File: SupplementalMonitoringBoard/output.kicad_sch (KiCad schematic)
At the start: 7 parts

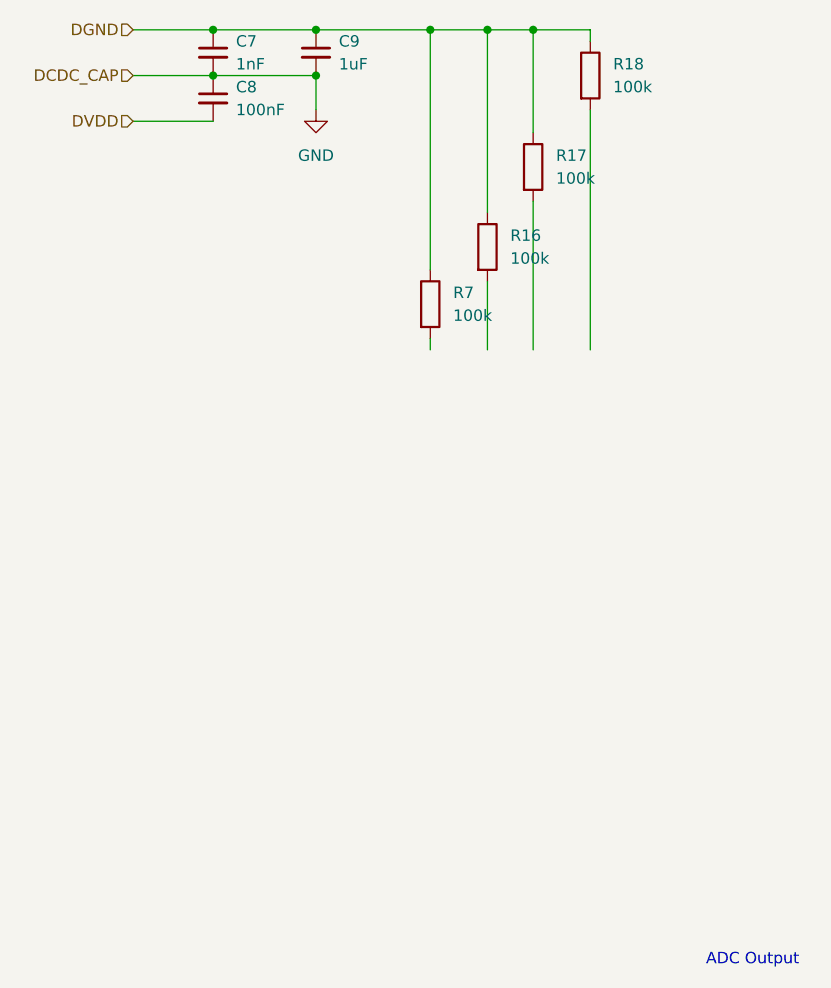
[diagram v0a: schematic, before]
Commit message: Supplemental Monitoring Board Changes
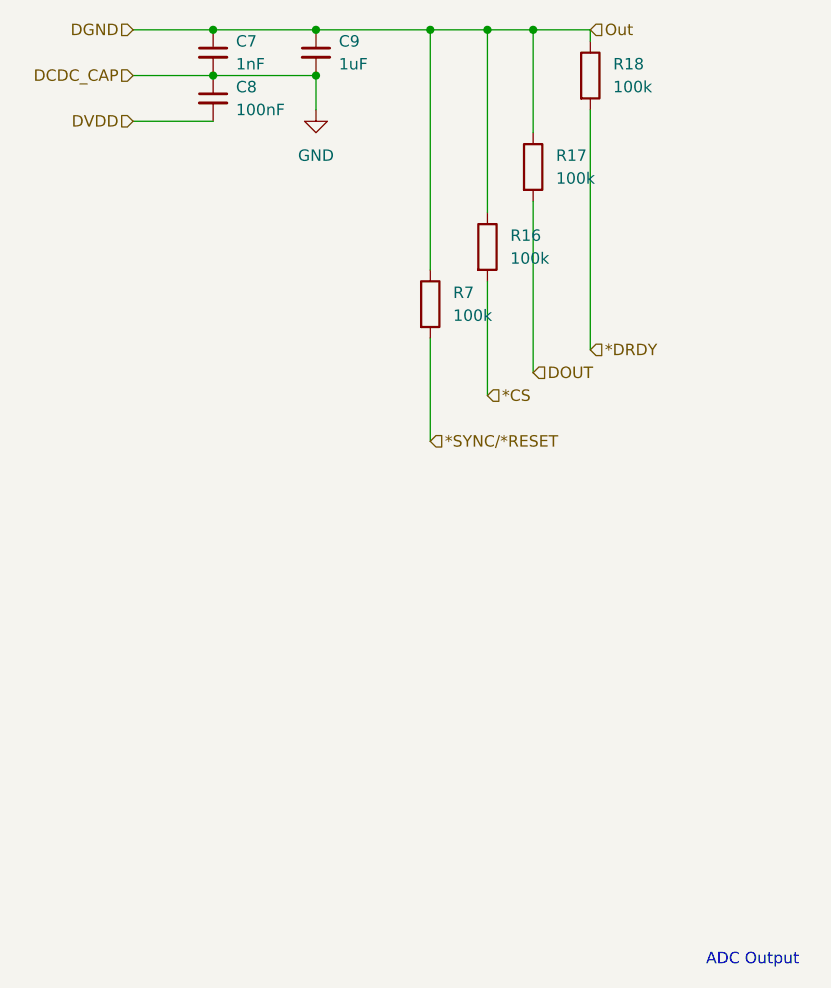
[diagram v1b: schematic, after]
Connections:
- net *CS: now reaches R16.2
- net *DRDY: now reaches R18.2
- net *SYNC/*RESET: now reaches R7.2
- net DOUT: now reaches R17.2
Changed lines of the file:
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@@
 	(wire
 		(pts
-			(xy 162.56 114.3) (xy 162.56 121.92)
+			(xy 162.56 114.3) (xy 162.56 127)
 		)
 		(stroke
@@
 	(wire
 		(pts
-			(xy 167.64 105.41) (xy 167.64 121.92)
+			(xy 167.64 105.41) (xy 167.64 124.46)
 		)
 		(stroke
@@
 	(wire
 		(pts
-			(xy 156.21 120.65) (xy 156.21 121.92)
+			(xy 156.21 120.65) (xy 156.21 132.08)
 		)
 		(stroke
@@
 		)
 	)
+	(hierarchical_label "*CS"
+		(shape input)
+		(at 162.56 127 0)
+		(fields_autoplaced yes)
+		(effects
+			(font
+				(size 1.27 1.27)
+			)
+			(justify left)
+		)
+	)
+	(hierarchical_label "*DRDY"
+		(shape input)
+		(at 173.99 121.92 0)
+		(fields_autoplaced yes)
+		(effects
+			(font
+				(size 1.27 1.27)
+			)
+			(justify left)
+		)
+	)
+	(hierarchical_label "*SYNC{slash}*RESET"
+		(shape input)
+		(at 156.21 132.08 0)
+		(fields_autoplaced yes)
+		(effects
+			(font
+				(size 1.27 1.27)
+			)
+			(justify left)
+		)
+	)
 	(hierarchical_label "DCDC_CAP"
 		(shape input)
@@
 		)
 	)
+	(hierarchical_label "DOUT"
+		(shape input)
+		(at 167.64 124.46 0)
+		(fields_autoplaced yes)
+		(effects
+			(font
+				(size 1.27 1.27)
+			)
+			(justify left)
+		)
+	)
+	(hierarchical_label "Out"
+		(shape input)
+		(at 173.99 86.36 0)
+		(fields_autoplaced yes)
+		(effects
+			(font
+				(size 1.27 1.27)
+			)
+			(justify left)
+		)
+	)

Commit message: thing
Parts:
- C7, C8, C9: footprint (none) -> Capacitor_SMD:C_0805_2012Metric
- R16, R17, R18, R7: footprint (none) -> Resistor_SMD:R_0805_2012Metric
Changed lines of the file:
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@@
 			)
 		)
-		(property "Footprint" ""
+		(property "Footprint" "Resistor_SMD:R_0805_2012Metric"
 			(at 160.782 110.49 90)
 			(effects
@@
 			)
 		)
-		(property "Footprint" ""
+		(property "Footprint" "Capacitor_SMD:C_0805_2012Metric"
 			(at 143.51 88.9 0)
 			(effects
@@
 			)
 		)
-		(property "Footprint" ""
+		(property "Footprint" "Resistor_SMD:R_0805_2012Metric"
 			(at 172.212 91.44 90)
 			(effects
@@
 			)
 		)
-		(property "Footprint" ""
+		(property "Footprint" "Capacitor_SMD:C_0805_2012Metric"
 			(at 132.08 93.98 0)
 			(effects
@@
 			)
 		)
-		(property "Footprint" ""
+		(property "Footprint" "Resistor_SMD:R_0805_2012Metric"
 			(at 154.432 116.84 90)
 			(effects
@@
 			)
 		)
-		(property "Footprint" ""
+		(property "Footprint" "Capacitor_SMD:C_0805_2012Metric"
 			(at 132.08 88.9 0)
 			(effects
@@
 			)
 		)
-		(property "Footprint" ""
+		(property "Footprint" "Resistor_SMD:R_0805_2012Metric"
 			(at 165.862 101.6 90)
 			(effects

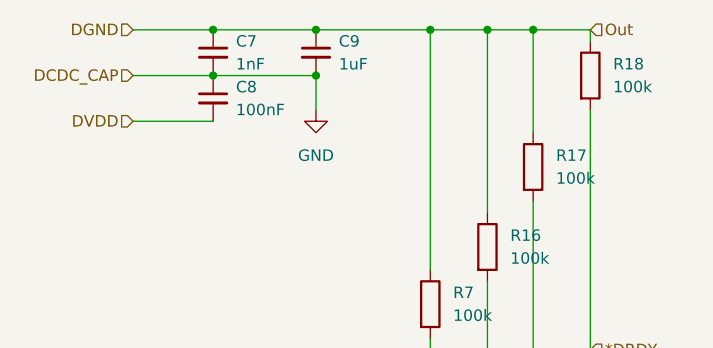
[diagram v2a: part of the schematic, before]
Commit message: Adressed Reviews - Supplemental Monitoring Board
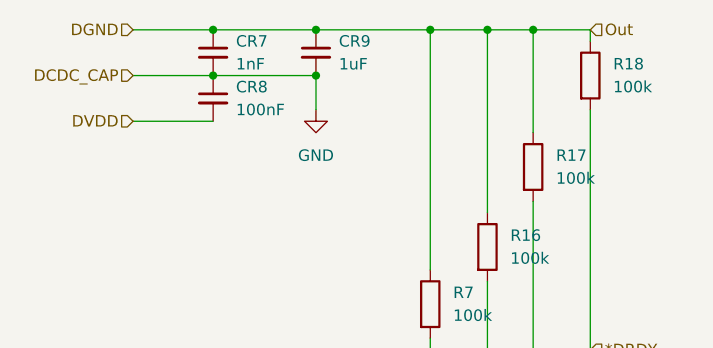
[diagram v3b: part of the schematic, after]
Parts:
- renumbered C7 to CR7, C8 to CR8, C9 to CR9
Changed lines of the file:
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@@
 		(dnp no)
 		(fields_autoplaced yes)
-		(property "Reference" "C9"
+		(property "Reference" "CR9"
 			(at 146.05 87.6362 0)
 			(effects
@@
 			(project "SupplementalMonitoringBoard"
 				(path "/aa0415d0-3287-4bc4-9a8e-766ada9ace2f/1227ac4e-31e5-4c8e-a2fc-47c8873f33fc"
-					(reference "C9")
+					(reference "CR9")
 					(unit 1)
 				)
@@
 		(dnp no)
 		(fields_autoplaced yes)
-		(property "Reference" "C8"
+		(property "Reference" "CR8"
 			(at 134.62 92.7162 0)
 			(effects
@@
 			(project "SupplementalMonitoringBoard"
 				(path "/aa0415d0-3287-4bc4-9a8e-766ada9ace2f/1227ac4e-31e5-4c8e-a2fc-47c8873f33fc"
-					(reference "C8")
+					(reference "CR8")
 					(unit 1)
 				)
@@
 		(dnp no)
 		(fields_autoplaced yes)
-		(property "Reference" "C7"
+		(property "Reference" "CR7"
 			(at 134.62 87.6362 0)
 			(effects
@@
 			(project "SupplementalMonitoringBoard"
 				(path "/aa0415d0-3287-4bc4-9a8e-766ada9ace2f/1227ac4e-31e5-4c8e-a2fc-47c8873f33fc"
-					(reference "C7")
-					(unit 1)
-				)
+					(reference "CR7")
+					(unit 1)
+				)
